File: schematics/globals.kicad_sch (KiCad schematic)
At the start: 33 parts, among them J1 Power, U1 74HCU04, U2 74HC14, U3 ATF22V10C-7, U4 74HC590, U5 74HC590, U6 74HC590, U7 PicoROM32, Y1 12M

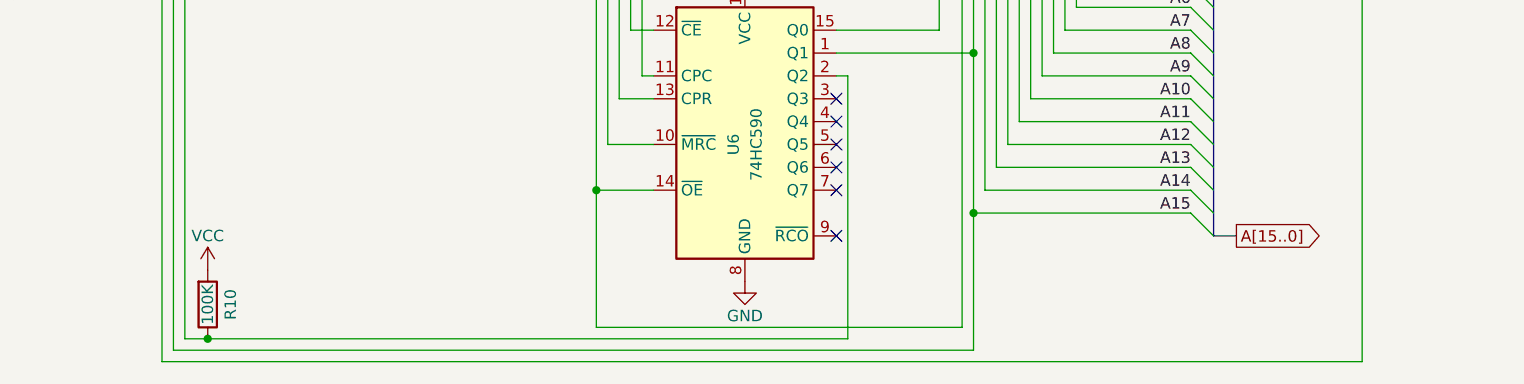
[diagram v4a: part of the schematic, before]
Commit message: added some picorom and pld writing stuff to makefiles
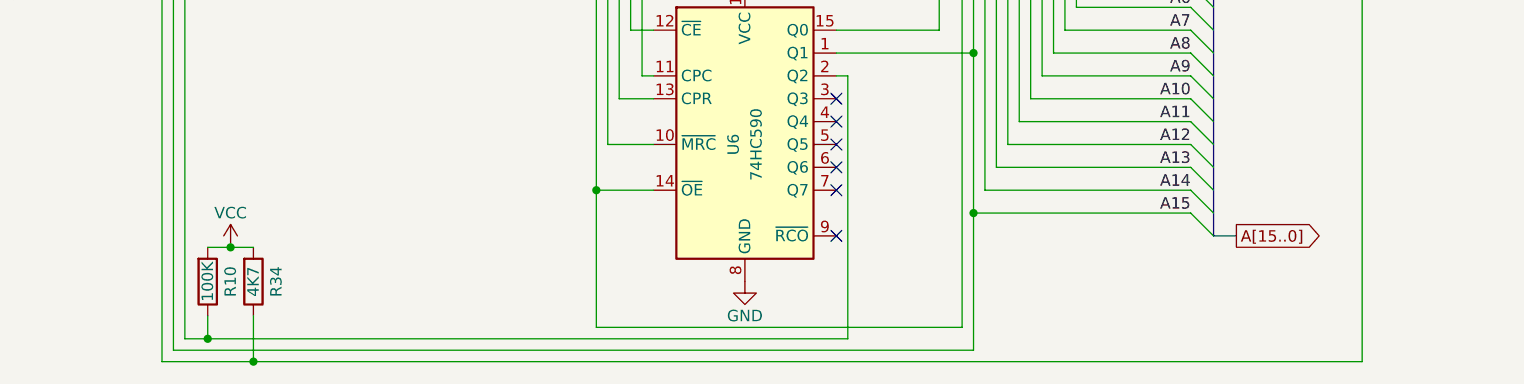
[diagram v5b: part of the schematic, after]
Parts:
- added R34: 4K7, symbol Device:R
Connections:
- net VCC: now also R34.2
- net at U3.7 (~{R_IN2}), U7.J0 (RL): now also R34.1
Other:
- moved on the sheet: R10
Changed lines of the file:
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@@
 	)
 	(junction
+		(at 119.38 165.1)
+		(diameter 0)
+		(color 0 0 0 0)
+	)
+	(junction
 		(at 97.79 64.77)
 		(diameter 0)
@@
 	)
 	(junction
+		(at 121.92 154.94)
+		(diameter 0)
+		(color 0 0 0 0)
+	)
+	(junction
 		(at 36.83 25.4)
 		(diameter 0)
@@
 	)
 	(junction
-		(at 119.38 165.1)
-		(diameter 0)
-		(color 0 0 0 0)
-	)
-	(junction
 		(at 139.7 62.23)
 		(diameter 0)
@@
 	)
 	(junction
+		(at 124.46 167.64)
+		(diameter 0)
+		(color 0 0 0 0)
+	)
+	(junction
 		(at 217.17 62.23)
 		(diameter 0)
@@
 	(wire
 		(pts
+			(xy 124.46 167.64) (xy 114.3 167.64)
+		)
+		(stroke
+			(width 0)
+			(type default)
+		)
+	)
+	(wire
+		(pts
 			(xy 224.79 90.17) (xy 224.79 92.71)
 		)
@@
 	(wire
 		(pts
+			(xy 121.92 154.94) (xy 119.38 154.94)
+		)
+		(stroke
+			(width 0)
+			(type default)
+		)
+	)
+	(wire
+		(pts
 			(xy 189.23 100.33) (xy 196.85 100.33)
 		)
@@
 	(wire
 		(pts
+			(xy 121.92 154.94) (xy 124.46 154.94)
+		)
+		(stroke
+			(width 0)
+			(type default)
+		)
+	)
+	(wire
+		(pts
 			(xy 40.64 125.73) (xy 40.64 127)
 		)
@@
 	(wire
 		(pts
+			(xy 124.46 162.56) (xy 124.46 167.64)
+		)
+		(stroke
+			(width 0)
+			(type default)
+		)
+	)
+	(wire
+		(pts
 			(xy 189.23 54.61) (xy 220.98 54.61)
 		)
@@
 	(wire
 		(pts
+			(xy 119.38 162.56) (xy 119.38 165.1)
+		)
+		(stroke
+			(width 0)
+			(type default)
+		)
+	)
+	(wire
+		(pts
 			(xy 163.83 143.51) (xy 163.83 100.33)
 		)
@@
 	(wire
 		(pts
-			(xy 247.65 167.64) (xy 114.3 167.64)
+			(xy 247.65 167.64) (xy 124.46 167.64)
 		)
 		(stroke
@@
 	(symbol
 		(lib_id "power:VCC")
-		(at 119.38 157.48 0)
+		(at 121.92 154.94 0)
 		(unit 1)
 		(body_style 1)
@@
 		(dnp no)
 		(property "Reference" "#PWR010"
-			(at 119.38 161.29 0)
+			(at 121.92 158.75 0)
 			(hide yes)
 			(show_name no)
@@
 		)
 		(property "Value" "VCC"
-			(at 119.38 153.67 0)
+			(at 121.92 151.13 0)
 			(show_name no)
 			(do_not_autoplace no)
@@
 		)
 		(property "Footprint" ""
-			(at 119.38 157.48 0)
+			(at 121.92 154.94 0)
 			(hide yes)
 			(show_name no)
@@
 		)
 		(property "Datasheet" ""
-			(at 119.38 157.48 0)
+			(at 121.92 154.94 0)
 			(hide yes)
 			(show_name no)
@@
 		)
 		(property "Description" "Power symbol creates a global label with name \"VCC\""
-			(at 119.38 157.48 0)
+			(at 121.92 154.94 0)
 			(hide yes)
 			(show_name no)
@@
 	(symbol
 		(lib_id "Device:R")
-		(at 119.38 161.29 0)
+		(at 119.38 158.75 0)
 		(mirror x)
 		(unit 1)
@@
 		(dnp no)
 		(property "Reference" "R10"
-			(at 121.92 161.29 90)
+			(at 121.92 158.75 90)
 			(show_name no)
 			(do_not_autoplace no)
@@
 		)
 		(property "Value" "100K"
-			(at 119.38 161.29 90)
+			(at 119.38 158.75 90)
 			(show_name no)
 			(do_not_autoplace no)
@@
 		)
 		(property "Footprint" ""
-			(at 117.602 161.29 90)
+			(at 117.602 158.75 90)
 			(hide yes)
 			(show_name no)
@@
 		)
 		(property "Datasheet" ""
-			(at 119.38 161.29 0)
+			(at 119.38 158.75 0)
 			(hide yes)
 			(show_name no)
@@
 		)
 		(property "Description" "Resistor"
-			(at 119.38 161.29 0)
+			(at 119.38 158.75 0)
 			(hide yes)
 			(show_name no)
@@
 					(unit 1)
 				)
+			)
+		)
+	)
+	(symbol
+		(lib_id "Device:R")
+		(at 124.46 158.75 0)
+		(mirror x)
+		(unit 1)
+		(body_style 1)
+		(exclude_from_sim no)
+		(in_bom yes)
+		(on_board yes)
+		(in_pos_files yes)
+		(dnp no)
+		(property "Reference" "R34"
+			(at 127 158.75 90)
+			(show_name no)
+			(do_not_autoplace no)
+			(effects
+				(font
+					(size 1.27 1.27)
+				)
+			)
+		)
+		(property "Value" "4K7"
+			(at 124.46 158.75 90)
+			(show_name no)
+			(do_not_autoplace no)
+			(effects
+				(font
+					(size 1.27 1.27)
+				)
+			)
+		)
+		(property "Footprint" ""
+			(at 122.682 158.75 90)
+			(hide yes)
+			(show_name no)
+			(do_not_autoplace no)
+			(effects
+				(font
+					(size 1.27 1.27)
+				)
+			)
+		)
+		(property "Datasheet" ""
+			(at 124.46 158.75 0)
+			(hide yes)
+			(show_name no)
+			(do_not_autoplace no)
+			(effects
+				(font
+					(size 1.27 1.27)
+				)
+			)
+		)
+		(property "Description" "Resistor"
+			(at 124.46 158.75 0)
+			(hide yes)
+			(show_name no)
+			(do_not_autoplace no)
+			(effects
+				(font
+					(size 1.27 1.27)
+				)
+			)
+		)
+		(pin "2"
+		)
+		(pin "1"
+		)
+		(instances
+			(project "bv6502_hw"
+				(path "/94c72abe-aaa5-49aa-8ab7-5d3e7cbc10be/560ef1bd-4b3f-459c-9f6a-9898850b3c5b"
+					(reference "R34")
+					(unit 1)
+				)

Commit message: idk
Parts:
- R11: value 1K -> 2K2
- R4, R44: value 1K -> 4K7
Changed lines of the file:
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@@
 			)
 		)
-		(property "Value" "1K"
+		(property "Value" "4K7"
 			(at 153.67 74.93 90)
 			(show_name no)
@@
 			)
 		)
-		(property "Value" "1K"
+		(property "Value" "2K2"
 			(at 139.7 74.93 90)
 			(show_name no)
@@
 			)
 		)
-		(property "Value" "1K"
+		(property "Value" "4K7"
 			(at 104.14 87.63 90)
 			(show_name no)

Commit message: clock improvements
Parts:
- added Q6, Q7: 2N7000, Package_TO_SOT_THT:TO-92_Inline, symbol Transistor_FET:2N7000
- added R38, R9: 22R, symbol Device:R
- added U20: 74HC14, symbol 74xx:74HC14
- R11: value 2K2 -> 1K
- R2: value 470R -> 560R
- R44: value 4K7 -> 3K3
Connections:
- net GND: now also U2.1, U2.13, U2.3, Q6.1 (S), Q7.1 (S), U20.11, U20.13, U20.3, U20.7 (GND); no longer R11.2, R44.2, U2.5, U2.9
- net VCC: now also R11.2, R44.1, U20.14 (VCC)
- net ~{RES}: now also Q6.2 (G); no longer D5.2 (A)
- net at D17.1 (K): now also Q7.3 (D); no longer R44.1
- net at U3.19 (C.~{RS}), U4.10 (~{MRC}), U5.10 (~{MRC})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: now also Q7.2 (G); no longer D17.2 (A)
- net at U1.8: now also U20.5, U20.9; no longer U2.13
- net at C7.1, D2.2 (A), R5.2: now also U20.1; no longer U2.3
- net at U1.4, U1.5: now also U2.5, U2.9; no longer U2.1
- net at R11.1: now also D5.2 (A); no longer D5.1 (K)
- net at R7.1: now also U2.8; no longer U2.2
- net at U3.6 (~{R_IN1}): now also U20.2; no longer U2.4
- net at U2.12: no longer R8.1
- net ϕ0 renamed ϕ0.1
- net ϕ2 renamed ϕ2.1
- net ϕ2.1: now also R9.2; no longer R8.2
- new net: D17.2 (A), R44.2
- new net: R38.1, U20.6
- new net: R9.1, U20.8
- new net: D5.1 (K), Q6.3 (D)
- new net: R8.1, U2.6
- new net ϕ0.0: R8.2
- new net ϕ2.0: R38.2
- no-connect marks 12 -> 16
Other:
- note removed: "attaching cap to VCC instead of GND keeps it in reset until decoupoing caps are charged and power is stable...neat"
- moved on the sheet: C1, C2, C3, C4, C5, C6, C7, D1, D2, D5, J1, R1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

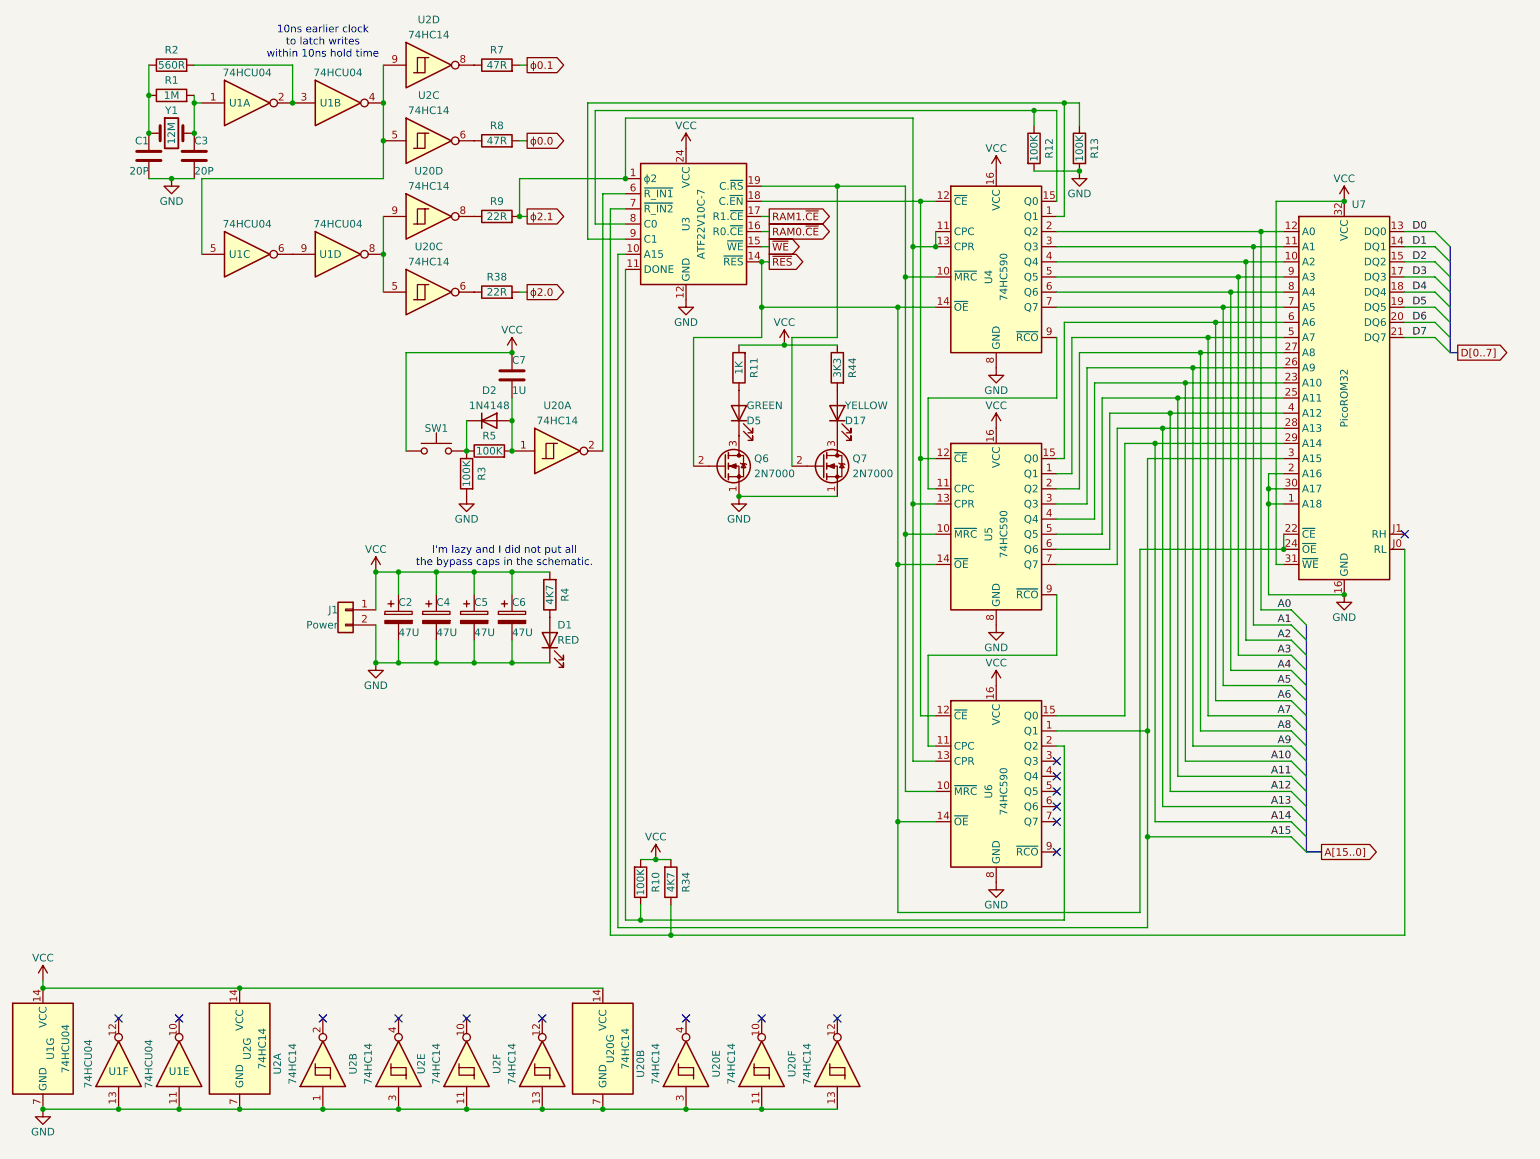
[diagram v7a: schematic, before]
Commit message: ditched phi0, dropped to 6MHz
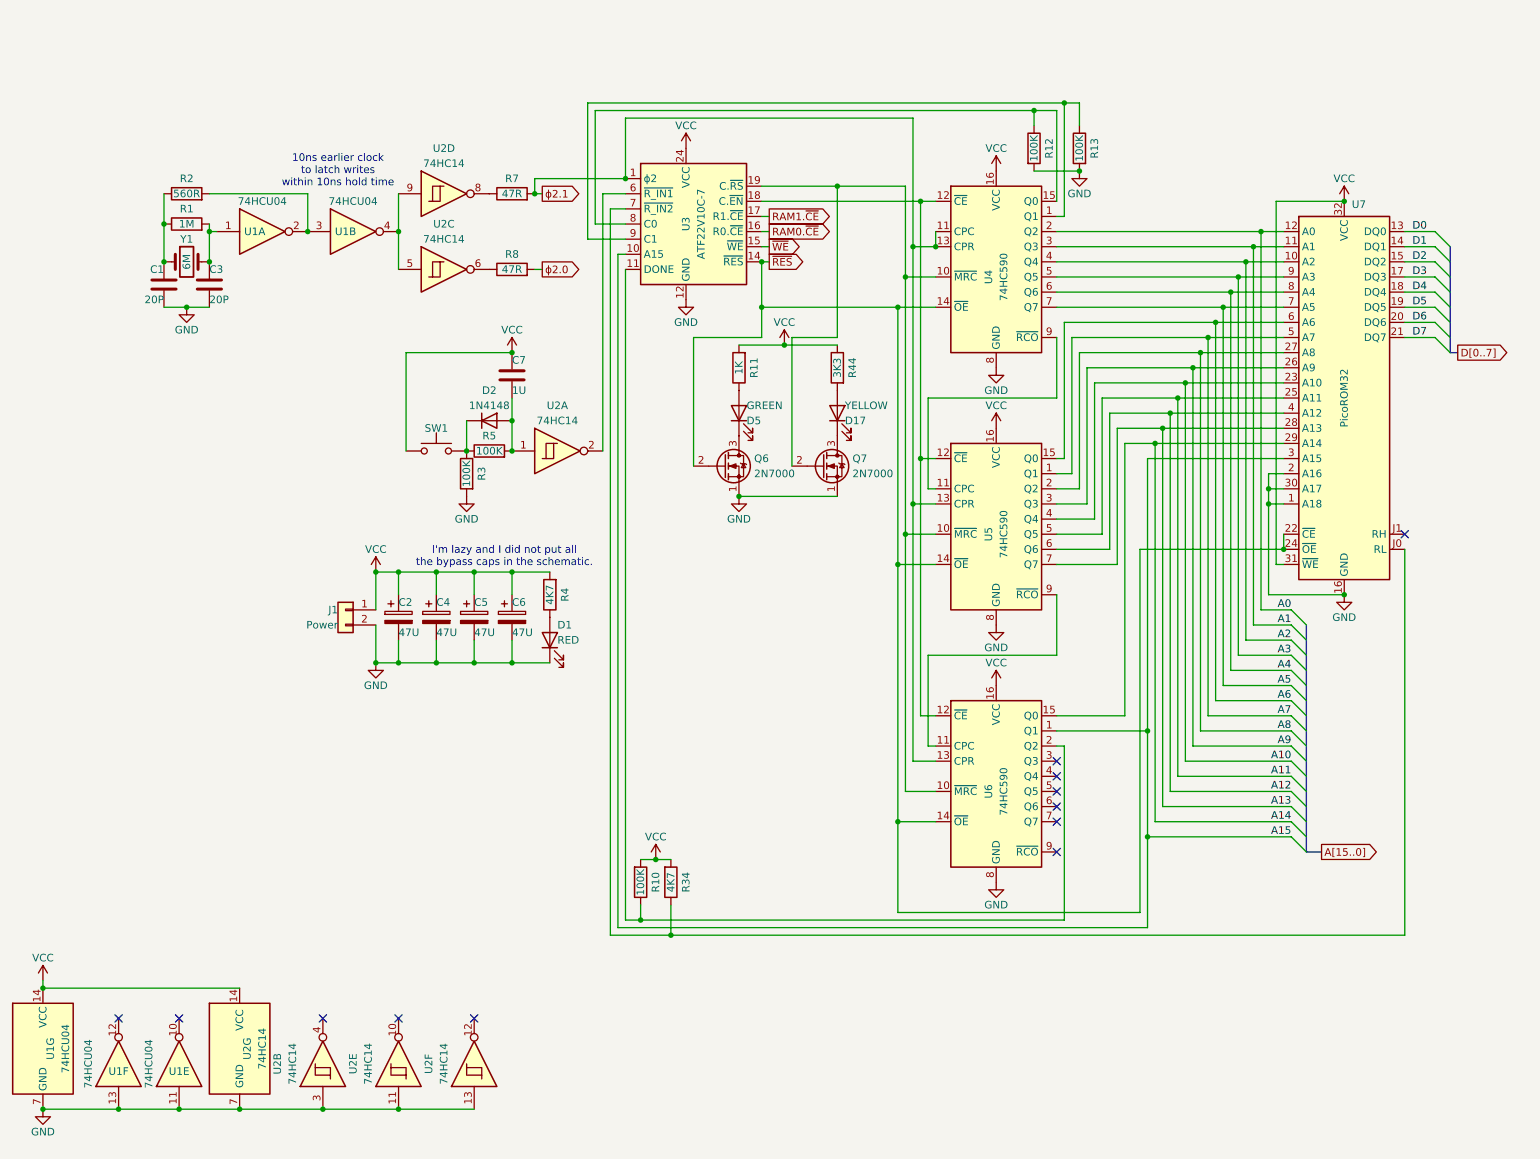
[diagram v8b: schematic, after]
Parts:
- removed R38, R9: 22R, symbol Device:R
- removed unit 4 of U1
- removed unit 3 of U1
- removed unit 2 of U2
- removed unit 3 of U20
- removed unit 4 of U20
- removed unit 7 of U20
- removed unit 5 of U20
- removed unit 6 of U20
- removed unit 2 of U20
- Y1: value 12M -> 6M
- renumbered U20 to U2
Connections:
- net ϕ0.0 is gone; now on net ϕ2.0: R8.2
- net ϕ0.1 is gone; now on net ϕ2.1: R7.2
- net GND: now also U2.3; no longer U2.1
- no-connect marks 16 -> 12
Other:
- moved on the sheet: C1, C3, R1, R2, R7, R8, U1A, U1B, U2C, U2D, U2E, U2F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
